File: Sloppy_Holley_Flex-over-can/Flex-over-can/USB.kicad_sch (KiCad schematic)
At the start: 4 parts, among them J2 USB-C, U9 USBLC6-2SC6

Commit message: Review power/connector sheets, fix ERC, add 3D models for all parts
- Remove duplicate PWR_FLAG on +5V (ERC pin_to_pin error)
- Register KiCad_Footprints and 24pinConnectorSymbol libs for J1
- Correct D1 value to B160-13-F and RV1 to SMDJ24CA to match LCSC parts
- C1: 10uF 50V X5R 1206 (C13585) for load-dump margin
- F2: 0.2A/60V resettable PTC, Brightking SMD1812B020TF-J (C269125)
- Add STEP models for J1, J2 (USB-C), SW1 (BOOT) and fix ESP32 model path
- Project-local footprint copies carry the models for J2, SW1, F2

Co-Authored-By: Claude Opus 5.5 <noreply@anthropic.com>
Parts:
- J2: footprint Connector_USB:USB_C_Receptacle_HRO_TYPE-C-31-M-12 -> KiCad_Footprints:USB_C_Receptacle_HRO_TYPE-C-31-M-12
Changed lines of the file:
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@@
 			)
 		)
-		(property "Footprint" "Connector_USB:USB_C_Receptacle_HRO_TYPE-C-31-M-12"
+		(property "Footprint" "KiCad_Footprints:USB_C_Receptacle_HRO_TYPE-C-31-M-12"
 			(at 63.5 101.6 0)
 			(hide yes)

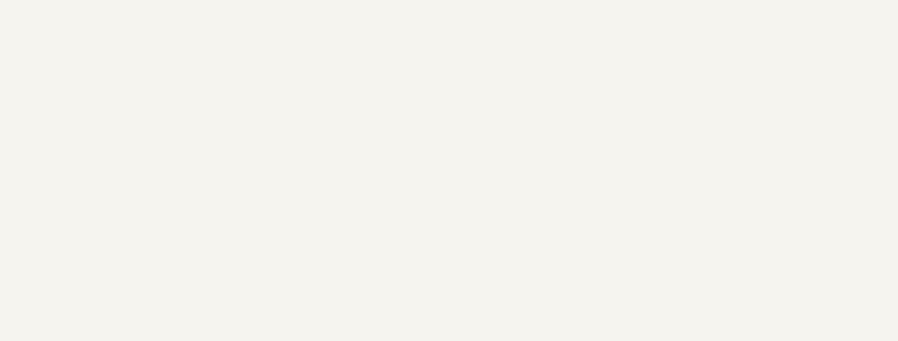
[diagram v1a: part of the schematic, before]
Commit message: Add PCB placement notes for decoupling caps to each sheet
Co-Authored-By: Claude Opus 5.5 <noreply@anthropic.com>
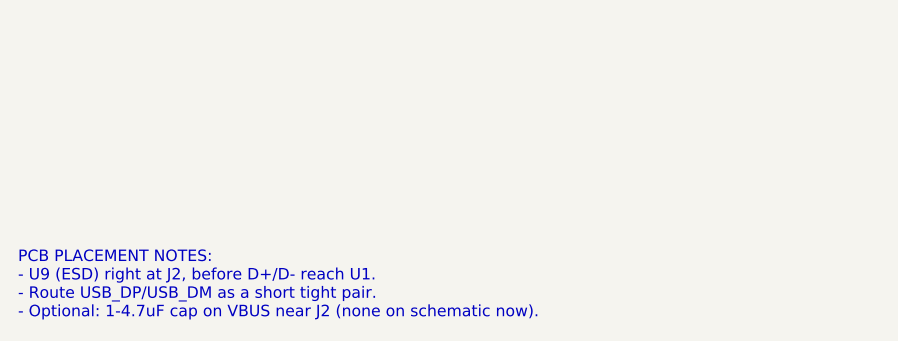
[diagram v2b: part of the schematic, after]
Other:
- note added: "PCB PLACEMENT NOTES: - U9 (ESD) right at J2, before D+/D- reach U1. - Route USB_DP/USB_DM as a short tight pair. - Optional: 1-4.7uF cap on VBUS near J2 (none on schematic now)."
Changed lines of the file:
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@@
 		)
 	)
+  (text "PCB PLACEMENT NOTES:\n- U9 (ESD) right at J2, before D+/D- reach U1.\n- Route USB_DP/USB_DM as a short tight pair.\n- Optional: 1-4.7uF cap on VBUS near J2 (none on schematic now)."
+    (at 15.24 180.34 0)
+    (effects (font (size 1.27 1.27) (color 0 0 194 1)) (justify left bottom))
+  )
 	(symbol
 		(lib_id "Power_Protection:USBLC6-2SC6")
